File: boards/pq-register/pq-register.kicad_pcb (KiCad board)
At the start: 2 copper layers, 114.3 x 127 mm, 688 parts, among them P1 Card Edge, Q1 MMBT5401, Q10 MMBT5401, Q100 MMBT5401, Q101 MMBT5401, Q102 MMBT5401, Q103 MMBT5401, Q11 MMBT5401, Q12 MMBT5401, Q13 MMBT5401, Q14 MMBT5401, Q15 MMBT5401, Q16 MMBT5401, Q17 MMBT5401, Q18 MMBT5401, Q19 MMBT5401, Q2 MMBT5401, Q20 MMBT5401, Q21 MMBT5401, Q22 MMBT5401, Q23 MMBT5401, Q24 MMBT5401, Q25 MMBT5401, Q26 MMBT5401, Q27 MMBT5401, Q28 MMBT5401, Q29 MMBT5401, Q3 MMBT5401, Q30 MMBT5401, Q31 MMBT5401, Q32 MMBT5401, Q33 MMBT5401, Q34 MMBT5401, Q35 MMBT5401, Q36 MMBT5401, Q37 MMBT5401, Q38 MMBT5401, Q39 MMBT5401, Q4 MMBT5401, Q40 MMBT5401, Q41 MMBT5401, Q42 MMBT5401, Q43 MMBT5401, Q44 MMBT5401, Q45 MMBT5401, Q46 MMBT5401, Q47 MMBT5401, Q48 MMBT5401, Q49 MMBT5401, Q5 MMBT5401, Q50 MMBT5401, Q51 MMBT5401, Q52 MMBT5401, Q53 MMBT5401, Q54 MMBT5401, Q55 MMBT5401, Q56 MMBT5401, Q57 MMBT5401, Q58 MMBT5401, Q59 MMBT5401, Q6 MMBT5401, Q60 MMBT5401, Q61 MMBT5401, Q62 MMBT5401, Q63 MMBT5401, Q64 MMBT5401, Q65 MMBT5401, Q66 MMBT5401, Q67 MMBT5401, Q68 MMBT5401, Q69 MMBT5401, Q7 MMBT5401, Q70 MMBT5401, Q71 MMBT5401, Q72 MMBT5401, Q73 MMBT5401, Q74 MMBT5401, Q75 MMBT5401, Q76 MMBT5401, Q77 MMBT5401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

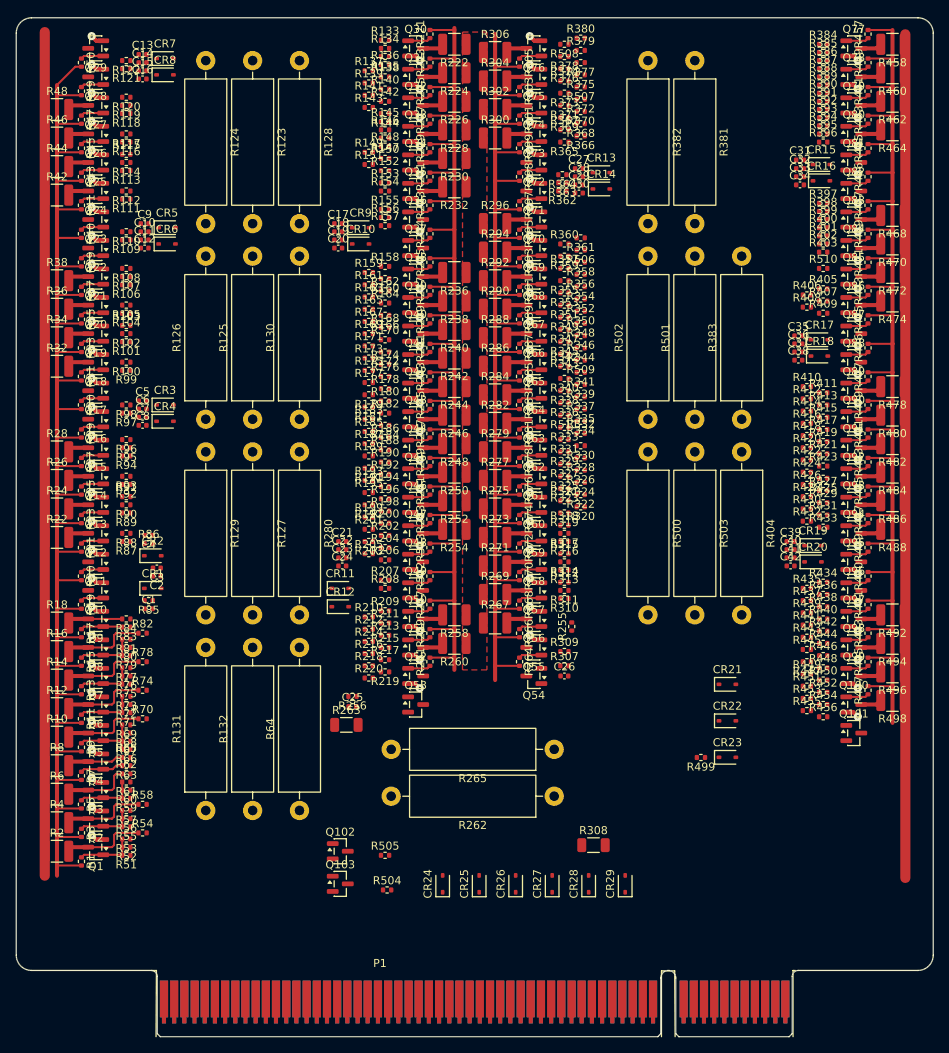
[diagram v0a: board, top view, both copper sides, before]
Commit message: Better PCI footprint, more layout.
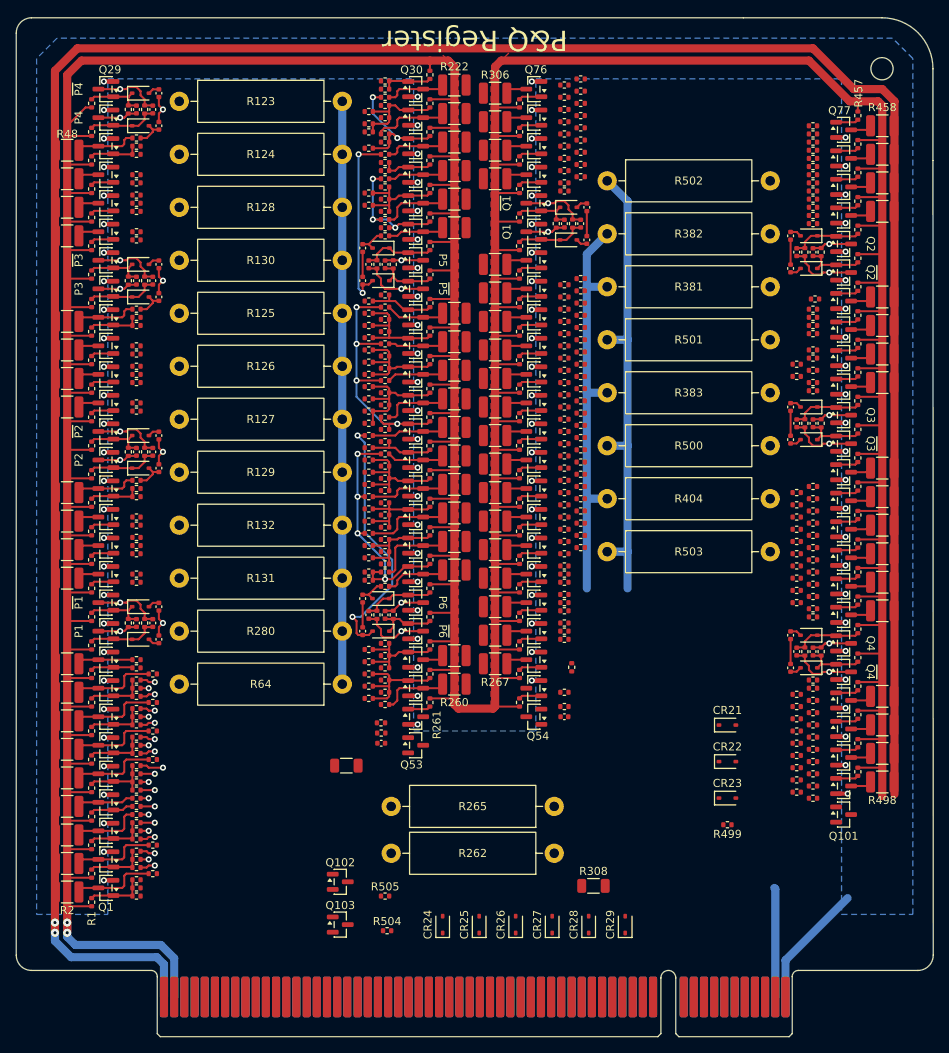
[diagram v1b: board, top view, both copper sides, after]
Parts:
- added MH1: Bivar CP-26 WE, Project:Bivar_CP-26_WE, B.Cu at (184.1, 57.1)
- P1: footprint Connector_PCBEdge:BUS_PCI -> Project:Bus_PCI_5V_32bit
- moved R132 37.3 mm to (116.8, 114.0), turned to 180 degrees
- moved R131 33.6 mm to (116.8, 120.7), turned to 180 degrees
- moved R381 30.2 mm to (149.9, 84.3), turned to 0 degrees
- moved R502 30.1 mm to (149.9, 71.1), turned to 0 degrees
- moved R280 23.0 mm to (116.8, 127.3), turned to 180 degrees
- moved R382 22.2 mm to (149.9, 77.7), turned to 0 degrees
- moved R124 20.6 mm to (116.8, 67.8), turned to 180 degrees
- moved R130 20.5 mm to (116.8, 81.0), turned to 180 degrees
- moved R128 19.0 mm to (116.8, 74.4), turned to 180 degrees
- moved R126 18.3 mm to (116.8, 94.2), turned to 180 degrees
- moved R404 17.8 mm to (149.9, 110.7), turned to 0 degrees
- moved R125 17.3 mm to (116.8, 87.6), turned to 180 degrees
- moved R129 17.2 mm to (116.8, 107.4), turned to 180 degrees
- moved R383 17.1 mm to (149.9, 97.5), turned to 0 degrees
- moved R64 16.6 mm to (116.8, 133.9), turned to 180 degrees
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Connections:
- net Net-(Q101-B) renamed /Q3/~{Q3_{S}}
- C10 pad 2: CP -> CP_{1}
- C11 pad 2: CP -> CP_{1}
- C14 pad 2: CP -> CP_{1}
- C15 pad 2: CP -> CP_{1}
- C18 pad 2: CP -> CP_{1}
- C19 pad 2: CP -> CP_{1}
- C2 pad 2: CP -> CP_{1}
- C22 pad 2: CP -> CP_{1}
- C23 pad 2: CP -> CP_{1}
- C28 pad 2: CP -> CP_{2}
- C29 pad 2: CP -> CP_{2}
- C3 pad 2: CP -> CP_{1}
- C32 pad 2: CP -> CP_{2}
- C33 pad 2: CP -> CP_{2}
- C36 pad 2: CP -> CP_{2}
- C37 pad 2: CP -> CP_{2}
- C40 pad 2: CP -> CP_{2}
- C41 pad 2: CP -> CP_{2}
- C6 pad 2: CP -> CP_{1}
- C7 pad 2: CP -> CP_{1}
- P1 pad A1: GND -> -20V
- P1 pad A10: ~{bq} -> ~{rl}
- P1 pad A11: ~{P4} -> ~{P1d}
- P1 pad A12: ~{P3} -> ~{P2c}
- P1 pad A13: ~{P2} -> ~{P2d}
- P1 pad A14: ~{H} -> ~{P3c}
- P1 pad A15: ~{S1} -> ~{P3d}
- P1 pad A16: ~{Q2d} -> ~{P4c}
- P1 pad A17: O1 -> ~{P4d}
- P1 pad A18: ~{Q2c} -> unconnected-(P1-~{Ac2}-PadA18)
- P1 pad A19: unconnected-(P1-~{S3}-PadA19) -> V
- P1 pad A2: -20V_{D} -> +15V
- P1 pad A20: ~{O1} -> ~{P5c}
- P1 pad A21: Q2a -> P5a
- P1 pad A22: ~{Q1d} -> ~{V}
- P1 pad A23: Q1b -> ~{P5d}
- P1 pad A24: unconnected-(P1-NC-PadA24) -> ~{P6c}
- P1 pad A25: Tc -> P6a
- P1 pad A26: ~{Tb4} -> ~{P6d}
- P1 pad A27: ~{Tb3} -> S2
- P1 pad A28: ~{ic} -> ia
- P1 pad A29: ~{Tb1} -> T3
- P1 pad A3: unconnected-(P1-~{W}-PadA3) -> ~{P1}
- P1 pad A30: ~{Tb2} -> S3
- P1 pad A31: S3 -> ~{Tb2}
- P1 pad A32: T3 -> ~{Tb1}
- P1 pad A33: ia -> ~{ic}
- P1 pad A34: S2 -> ~{Tb3}
- P1 pad A35: ~{P6d} -> ~{Tb4}
- P1 pad A36: P6a -> Tc
- P1 pad A37: ~{P6c} -> unconnected-(P1-PadA37)
- P1 pad A38: ~{P5d} -> Q1b
- P1 pad A39: ~{V} -> ~{Q1d}
- P1 pad A4: ~{Q3} -> -15V
- P1 pad A40: P5a -> Q2a
- P1 pad A41: ~{P5c} -> ~{O1}
- P1 pad A42: V -> unconnected-(P1-~{S3}-PadA42)
- P1 pad A43: unconnected-(P1-~{Ac2}-PadA43)_1 -> ~{Q2c}
- P1 pad A44: ~{P4d} -> O1
- P1 pad A45: ~{P4c} -> ~{Q2d}
- P1 pad A46: ~{P3d} -> ~{S1}
- P1 pad A47: ~{P3c} -> ~{H}
- P1 pad A48: ~{P2d} -> ~{P2}
- P1 pad A49: ~{P2c} -> ~{P3}
- P1 pad A5: Q3 -> P1
- P1 pad A52: ~{P1d} -> ~{P4}
- P1 pad A53: ~{rl} -> ~{bq}
- P1 pad A54: ~{P1c} -> ~{S2}
- P1 pad A55: rl -> ~{P5}
- P1 pad A56: ~{G} -> unconnected-(P1-W-PadA56)
- P1 pad A57: G -> Q1
- P1 pad A58: P1 -> Q3
- P1 pad A59: -15V -> ~{Q3}
- P1 pad A6: Q1 -> G
- P1 pad A60: ~{P1} -> unconnected-(P1-~{W}-PadA60)
- P1 pad A61: +15V -> -20V_{D}
- P1 pad A62: -20V -> GND
- P1 pad A7: unconnected-(P1-W-PadA7)_1 -> ~{G}
- P1 pad A8: ~{P5} -> rl
- P1 pad A9: ~{S2} -> ~{P1c}
- P1 pad B1: ~{Q4} -> P1b
- P1 pad B12: ~{To} -> unconnected-(P1-Aw'-PadB12)
- P1 pad B13: ~{Faf} -> ~{A}
- P1 pad B14: α9 -> A*
- P1 pad B15: ~{H'} -> ~{A*}
- P1 pad B16: ~{P6} -> A
- P1 pad B17: Q2 -> unconnected-(P1-Aa-PadB17)
- P1 pad B18: Q4 -> unconnected-(P1-~{T3}-PadB18)
- P1 pad B19: R -> P5
- P1 pad B2: ~{Q1} -> H
- P1 pad B20: ~{R} -> unconnected-(P1-~{brc}-PadB20)
- P1 pad B21: Faf -> unconnected-(P1-be-PadB21)
- P1 pad B22: B1 -> unconnected-(P1-~{be}-PadB22)
- P1 pad B24: ~{C} -> unconnected-(P1-~{Ac1}-PadB24)
- P1 pad B25: unconnected-(P1-K'-PadB25) -> F
- P1 pad B26: unconnected-(P1-~{K}-PadB26) -> ~{F}
- P1 pad B27: K -> CP
- P1 pad B28: unconnected-(P1-bq-PadB28)_1 -> P6
- P1 pad B29: P3 -> P2
- P1 pad B3: ~{Q2} -> unconnected-(P1-Fa-PadB3)
- P1 pad B30: P4 -> bs
- P1 pad B31: bs -> P4
- P1 pad B32: P2 -> P3
- P1 pad B33: P6 -> unconnected-(P1-bq-PadB33)
- P1 pad B34: Cp -> K
- P1 pad B35: ~{F} -> unconnected-(P1-~{K}-PadB35)
- P1 pad B36: F -> unconnected-(P1-K'-PadB36)
- P1 pad B37: unconnected-(P1-~{Ac1}-PadB37)_1 -> ~{C}
- P1 pad B39: unconnected-(P1-~{be}-PadB39)_1 -> B1
- P1 pad B40: unconnected-(P1-be-PadB40) -> Faf
- P1 pad B41: unconnected-(P1-~{brc}-PadB41) -> ~{R}
- P1 pad B42: P5 -> R
- P1 pad B43: unconnected-(P1-~{T3}-PadB43)_1 -> Q4
- P1 pad B44: unconnected-(P1-Aa-PadB44)_1 -> Q2
- P1 pad B45: A -> ~{P6}
- P1 pad B46: ~{A*} -> ~{H'}
- P1 pad B47: A* -> α9
- P1 pad B48: ~{A} -> ~{Faf}
- P1 pad B49: unconnected-(P1-Aw'-PadB49)_1 -> ~{To}
- P1 pad B60: unconnected-(P1-Fa-PadB60) -> ~{Q2}
- P1 pad B61: H -> ~{Q1}
- P1 pad B62: unconnected-(P1-P1b-PadB62) -> ~{Q4}
- Q53 pad 1: Cp -> CP
- Q54 pad 1: Cp -> CP
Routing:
- net -20V: track 210.3 -> 449.0 mm, vias 0 -> 2
- net +15V: track 645.2 -> 775.4 mm, vias 0 -> 2
- net -20V_{D}: track 0.00 -> 73.1 mm
- net Net-(CR12-A): track 0.00 -> 32.5 mm, vias 0 -> 2
- net Net-(Q42-B): track 2.85 -> 34.4 mm, vias 0 -> 4
- net GND: track 163.3 -> 132.3 mm
- net Net-(Q47-B): track 2.85 -> 31.7 mm, vias 0 -> 4
- net Net-(CR10-A): track 0.00 -> 22.8 mm, vias 0 -> 2
- net CP_{1}: track 0.00 -> 20.3 mm, vias 0 -> 4
- net Net-(Q32-B): track 2.85 -> 16.5 mm, vias 0 -> 2
- net Net-(Q35-B): track 2.85 -> 15.7 mm, vias 0 -> 3
- net Net-(Q41-B): track 2.85 -> 15.7 mm
- net CP_{2}: track 0.00 -> 12.4 mm
- net Net-(Q44-B): track 2.85 -> 15.1 mm
- net Net-(Q39-B): track 2.85 -> 14.2 mm
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- added copper zone on B.Cu, net GND
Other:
- board size 114.3 x 127 mm -> 114.3 x 118.7 mm
- board text added: "P&Q Register"
- board text added: "P1"
- board text added: "P2"
- board text added: "P3"
- board text added: "P4"
- board text added: "P5"
- board text added: "P6"
- board text added: "Q1"
- board text added: "Q2"
- board text added: "Q3"
- board text added: "Q4"
- board text added: "~{P1}"
- board text added: "~{P2}"
- board text added: "~{P3}"
- board text added: "~{P4}"
- board text added: "~{P5}"
- board text added: "~{P6}"
- board text added: "~{Q1}"
- board text added: "~{Q2}"
- board text added: "~{Q3}"
- board text added: "~{Q4}"

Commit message: More routing.
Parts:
- moved R362 7.62 mm to (144.5, 80.0)
- moved R508 2.87 mm to (146.6, 61.2)
- moved R506 2.54 mm to (144.5, 83.3)
- moved R379 2.40 mm to (144.5, 61.2)
- moved R361 2.27 mm to (144.5, 82.3)
- moved R83 2.09 mm to (93.2, 132.3)
- moved R82 2.05 mm to (91.2, 132.3)
- moved R374 1.52 mm to (144.5, 65.3)
- moved R375 1.52 mm to (146.6, 64.5)
- moved R365 1.52 mm to (144.5, 72.9)
- moved R366 1.52 mm to (146.6, 72.1)
- moved R367 1.52 mm to (144.5, 71.4)
- moved R368 1.52 mm to (146.6, 70.6)
- moved R369 1.52 mm to (144.5, 69.8)
- moved R370 1.52 mm to (146.6, 69.1)
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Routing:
- net Net-(CR2-A): track 2.45 -> 29.1 mm, vias 1 -> 2
- net Net-(Q76-B): track 2.85 -> 26.4 mm, vias 0 -> 3
- net Net-(Q9-B): track 5.24 -> 24.6 mm, vias 0 -> 4
- net Net-(CR6-A): track 1.43 -> 17.4 mm, vias 0 -> 2
- net Net-(CR4-A): track 1.43 -> 17.4 mm, vias 0 -> 2
- net Net-(Q74-B): track 2.85 -> 17.8 mm
- net Net-(Q4-B): track 6.41 -> 18.7 mm, vias 1 -> 3
- net Net-(Q75-B): track 2.85 -> 11.6 mm
- net Net-(Q26-C): track 2.64 -> 9.99 mm
- net Net-(Q20-C): track 2.64 -> 9.99 mm
- net Net-(Q14-C): track 2.64 -> 9.99 mm
- net Net-(Q12-C): track 2.64 -> 9.99 mm
- net Net-(Q18-C): track 2.64 -> 9.99 mm
- net Net-(Q24-C): track 2.64 -> 9.99 mm
- net P2: track 5.22 -> 12.4 mm, vias 1 -> 2
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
